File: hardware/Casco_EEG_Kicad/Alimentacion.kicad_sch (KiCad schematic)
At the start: 25 parts, among them J12 USB_B_Micro, Q1 FS8205A, U4 TP4056-42-ESOP8, U5 DW01A, U6 AMS1117-3.3

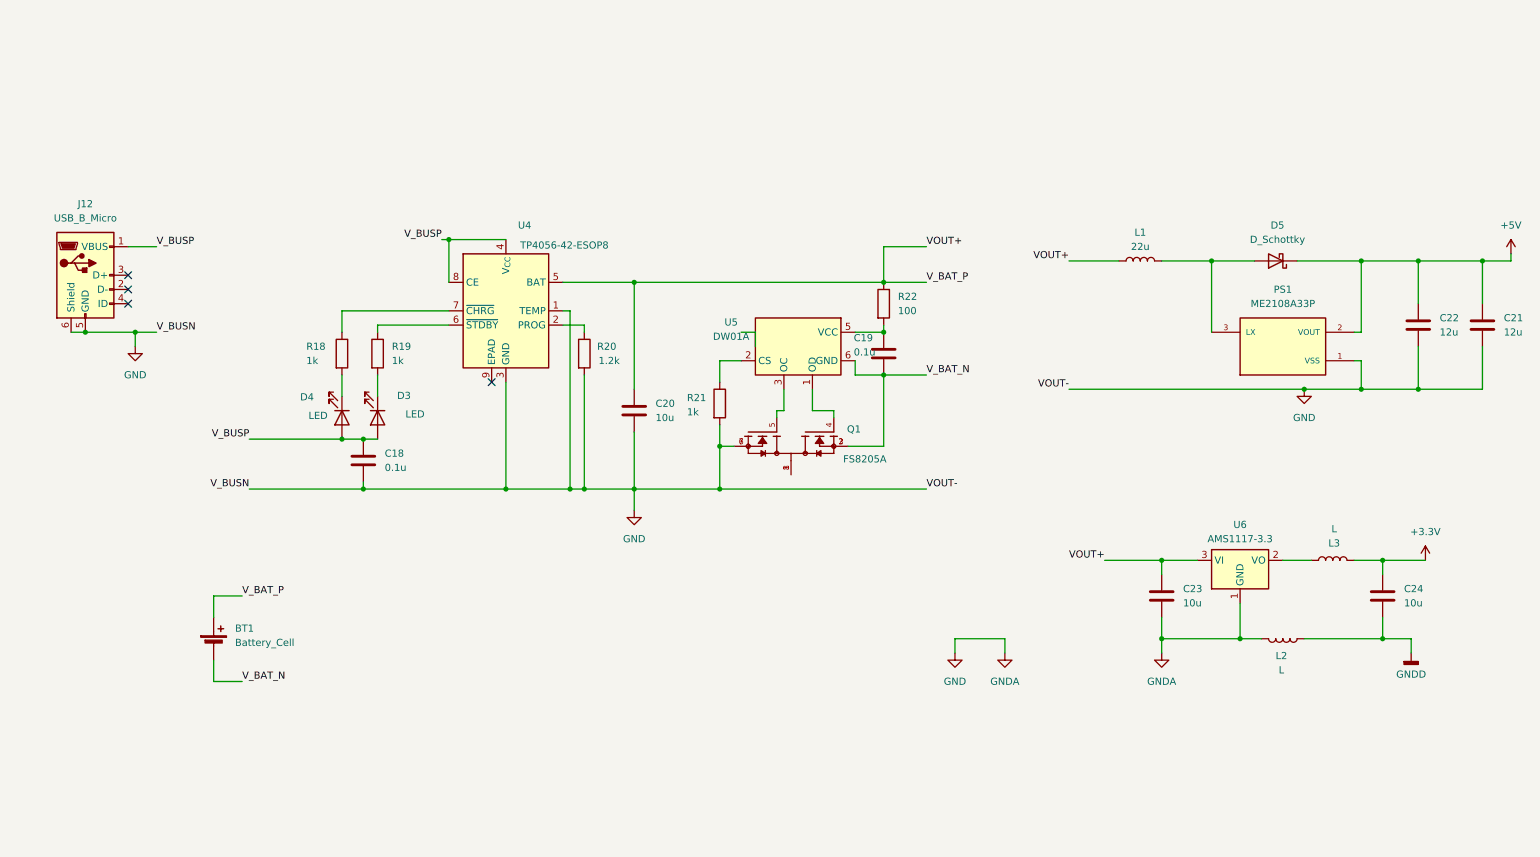
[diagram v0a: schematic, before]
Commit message: Primera implementacion de PCB, cambios varios
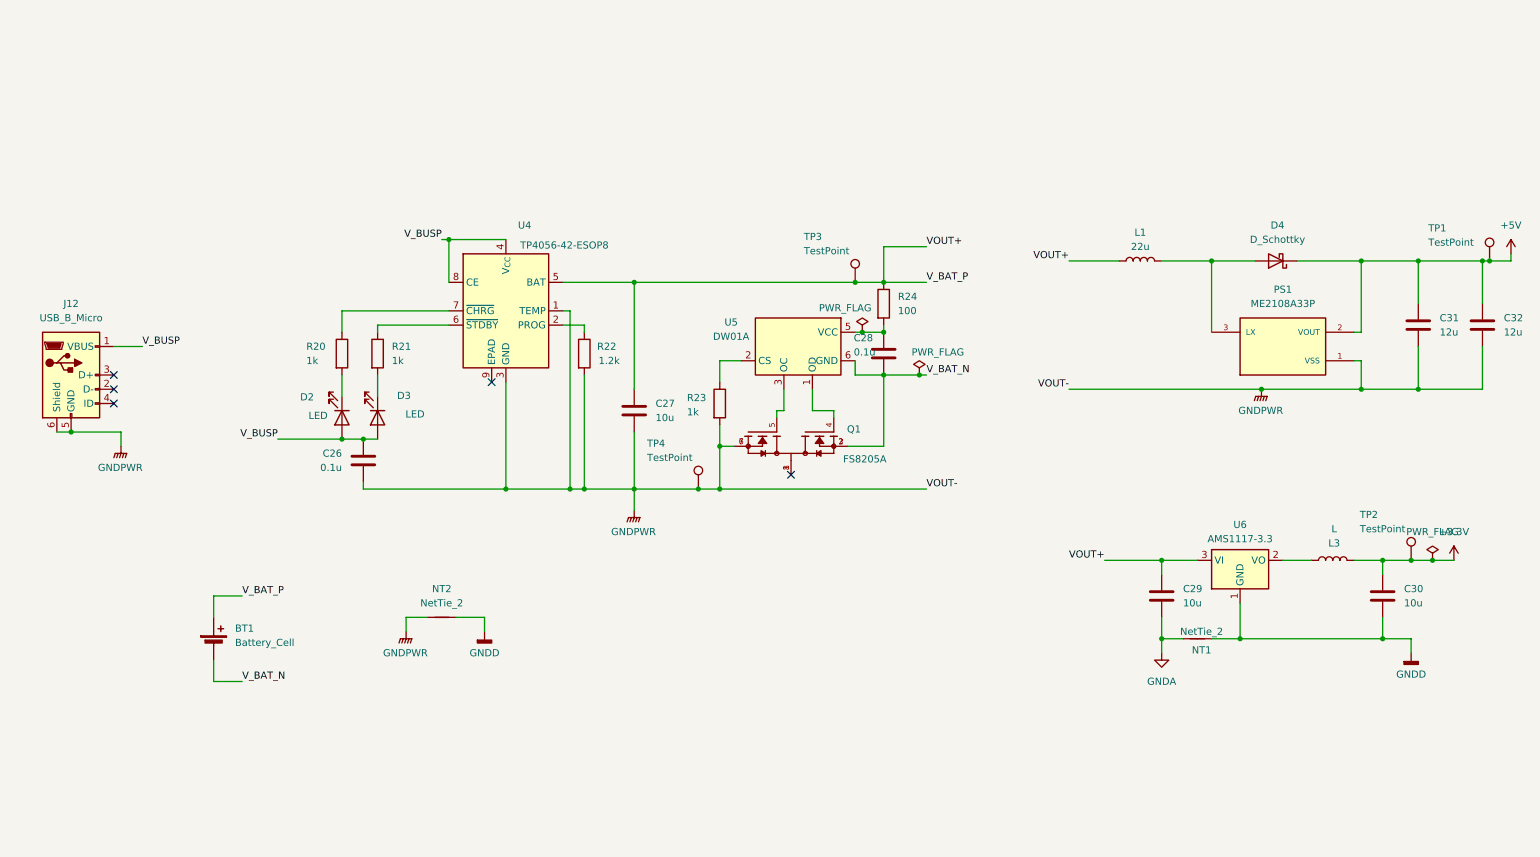
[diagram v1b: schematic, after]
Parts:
- removed L2: L, symbol Device:L
- added NT1, NT2: NetTie_2, NetTie:NetTie-2_SMD_Pad2.0mm, symbol Device:NetTie_2
- added TP1, TP2, TP3, TP4: TestPoint, TestPoint:TestPoint_Pad_D2.0mm, symbol Connector:TestPoint
- C26: renamed from C18; footprint (none) -> Capacitor_SMD:C_0603_1608Metric
- C27: renamed from C20; footprint (none) -> Capacitor_SMD:C_0603_1608Metric
- C28: renamed from C19; footprint (none) -> Capacitor_SMD:C_0603_1608Metric
- C29: renamed from C23; footprint (none) -> Capacitor_SMD:C_0603_1608Metric
- C30: renamed from C24; footprint (none) -> Capacitor_SMD:C_0603_1608Metric
- C31: renamed from C22; footprint (none) -> Capacitor_SMD:C_0805_2012Metric
- C32: renamed from C21; footprint (none) -> Capacitor_SMD:C_0805_2012Metric
- D2: renamed from D4; footprint (none) -> LED_SMD:LED_0603_1608Metric
- D3: footprint (none) -> LED_SMD:LED_0603_1608Metric
- D4: renamed from D5; footprint (none) -> Diode_SMD:D_SMA
- L1: footprint (none) -> Inductor_SMD:L_Coilcraft_XAL5030-XXX
- L3: footprint (none) -> Inductor_SMD:L_Coilcraft_LPS3010
- PS1: footprint ME2108A33P:CONV_ME2108A33P -> Huellas:CONV_ME2108A33P
- Q1: footprint FS8205A:SOP65P640X120-8N -> Huellas:SOP65P640X120-8N
- R20: renamed from R18; footprint (none) -> Resistor_SMD:R_0603_1608Metric
- R21: renamed from R19; footprint Resistor_SMD:R_0201_0603Metric -> Resistor_SMD:R_0603_1608Metric
- R22: renamed from R20; footprint (none) -> Resistor_SMD:R_0603_1608Metric
- R23: renamed from R21; footprint (none) -> Resistor_SMD:R_0603_1608Metric
- R24: renamed from R22; footprint (none) -> Resistor_SMD:R_0603_1608Metric
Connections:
- net +3.3V: now also TP2.1
- net +5V: now also TP1.1
- net GNDD: now also U6.1 (GND), NT1.2, NT2.2
- net VOUT+: now also TP3.1
- net GND renamed GNDPWR
- net GNDPWR: now also NT2.1, TP4.1; no longer C29.2, U6.1 (GND)
- new net GNDA: C29.2, NT1.1
- no-connect marks 4 -> 5
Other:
- moved on the sheet: J12

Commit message: Nuevos cambios al PCB, mejoro planos, regulo 3,3V desde 5V, etc
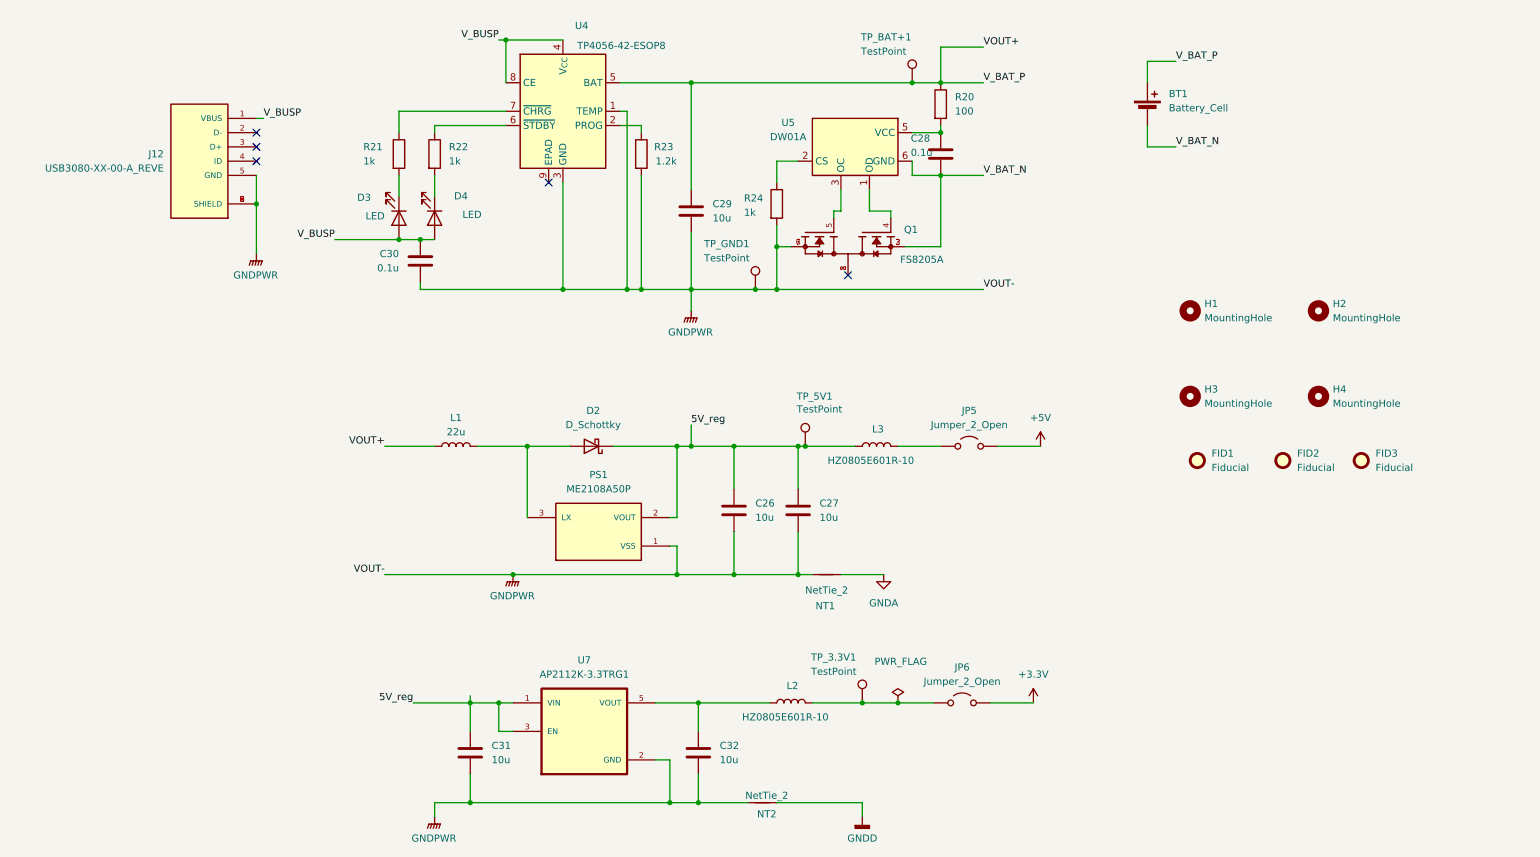
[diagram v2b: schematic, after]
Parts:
- removed J12: USB_B_Micro, Connector_USB:USB_Micro-AB_Molex_47590-0001, symbol Connector:USB_B_Micro
- removed U6: AMS1117-3.3, Package_TO_SOT_SMD:SOT-223-3_TabPin2, symbol Regulator_Linear:AMS1117-3.3
- added FID1, FID2, FID3: Fiducial, Fiducial:Fiducial_0.5mm_Mask1mm, symbol Mechanical:Fiducial
- added H1, H2, H3, H4: MountingHole, MountingHole:MountingHole_2.2mm_M2_Pad_Via, symbol Mechanical:MountingHole
- added J12: USB3080-XX-00-A_REVE, Huellas:GCT_USB3080-XX-00-A_REVE, symbol USBmicroB:USB3080-XX-00-A_REVE
- added JP5, JP6: Jumper_2_Open, Connector_PinHeader_2.54mm:PinHeader_1x02_P2.54mm_Vertical, symbol Jumper:Jumper_2_Open
- added L3: HZ0805E601R-10, Inductor_SMD:L_Eaton_MCL2012V1, symbol Device:L
- added U7: AP2112K-3.3TRG1, Huellas:SOT95P285X140-5N, symbol AP2112K-3.3:AP2112K-3.3TRG1
- C26: renamed from C31; value 12u -> 10u; LCSC PN (none) -> C19702
- C27: renamed from C32; value 12u -> 10u; LCSC PN (none) -> C19702
- C28: LCSC PN (none) -> C48579280
- C29: renamed from C27; LCSC PN (none) -> C19702
- C30: renamed from C26; LCSC PN (none) -> C48579280
- C31: renamed from C29; LCSC PN (none) -> C19702
- C32: renamed from C30; LCSC PN (none) -> C19702
- D2: renamed from D4; LCSC PN (none) -> C2480
- L2: renamed from L3; value L -> HZ0805E601R-10; footprint Inductor_SMD:L_Coilcraft_LPS3010 -> Inductor_SMD:L_Eaton_MCL2012V1; LCSC PN (none) -> C2441364
- PS1: value ME2108A33P -> ME2108A50P; Availability Not in stock -> (none); Check_prices https://www.snapeda.com/parts/ME2108A33P/Nanjing+Micro+One+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 -> (none); LCSC PN (none) -> C236798; MANUFACTURER Nanjing Micro One Electronics -> (none); MP ME2108A33P -> (none); PARTREV V10.0 -> (none); Package Package -> (none); Price None -> (none); STANDARD Manufacturer Recommendations -> (none)
- Q1: LCSC PN (none) -> C2830320
- R20: renamed from R24; LCSC PN (none) -> C22775
- R21: renamed from R20; LCSC PN (none) -> C22548
- R22: renamed from R21; LCSC PN (none) -> C22548
- R23: renamed from R22; LCSC PN (none) -> C22765
- R24: renamed from R23; LCSC PN (none) -> C22548
- U4: LCSC PN (none) -> C16581
- U5: LCSC PN (none) -> C2927799
- renumbered D2 to D3, D3 to D4, NT2 to NT1, NT1 to NT2, TP2 to TP_3.3V1, TP1 to TP_5V1, TP3 to TP_BAT+1, TP4 to TP_GND1
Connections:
- net +3.3V: now also JP6.2 (B); no longer C32.1, L2.2, TP_3.3V1.1
- net +5V: now also JP5.2 (B); no longer C26.1, C27.1, D2.1 (K), PS1.2 (VOUT), TP_5V1.1
- net GNDA: now also NT1.2; no longer C31.2, NT2.1
- net GNDD: no longer C32.2, NT1.2
- net GNDPWR: now also C31.2, C32.2, NT2.1, J12.5 (GND), J12.6 (SHIELD), J12.7 (SHIELD), J12.8 (SHIELD), J12.9 (SHIELD), U7.2 (GND)
- net VOUT+: no longer C31.1
- net V_BUSP: now also J12.1 (VBUS)
- net at L2.1: now also C32.1, U7.5 (VOUT)
- new net: JP5.1 (A), L3.2
- new net: JP6.1 (A), L2.2, TP_3.3V1.1
- new net 5V_reg: C26.1, C27.1, C31.1, D2.1 (K), L3.1, PS1.2 (VOUT), TP_5V1.1, U7.1 (VIN), U7.3 (EN)
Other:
- moved on the sheet: BT1, C26, C27, C28, C29, C30, C31, C32, D2, D3, D4, L1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

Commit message: Implemento pines I/O para trigger
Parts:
- C28, C30: LCSC PN C48579280 -> C14663
- R21, R22, R24: LCSC PN C22548 -> C21190
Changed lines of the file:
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@@
 			)
 		)
-		(property "LCSC PN" "C48579280"
+		(property "LCSC PN" "C14663"
 			(at 82.55 64.77 0)
 			(effects
@@
 			)
 		)
-		(property "LCSC PN" "C22548"
+		(property "LCSC PN" "C21190"
 			(at 146.05 54.61 0)
 			(effects
@@
 			)
 		)
-		(property "LCSC PN" "C48579280"
+		(property "LCSC PN" "C14663"
 			(at 175.26 45.72 0)
 			(effects
@@
 			)
 		)
-		(property "LCSC PN" "C22548"
+		(property "LCSC PN" "C21190"
 			(at 78.74 45.72 0)
 			(effects
@@
 			)
 		)
-		(property "LCSC PN" "C22548"
+		(property "LCSC PN" "C21190"
 			(at 85.09 45.72 0)
 			(effects

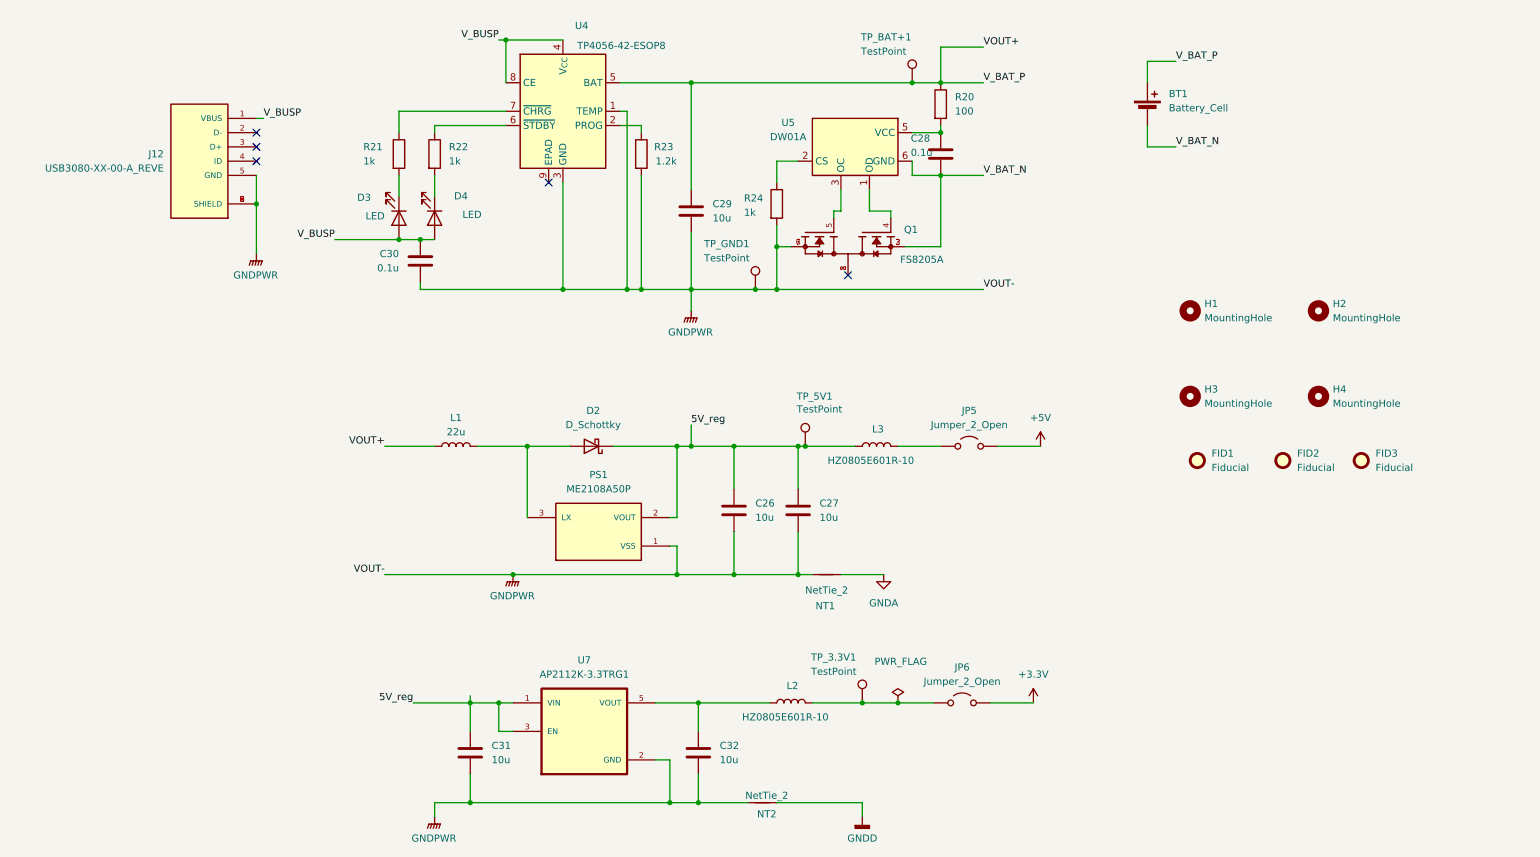
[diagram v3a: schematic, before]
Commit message: Actualizacion del modelo, agrego mini slide switch, agrego jumpers para comunicacion con modulo BT
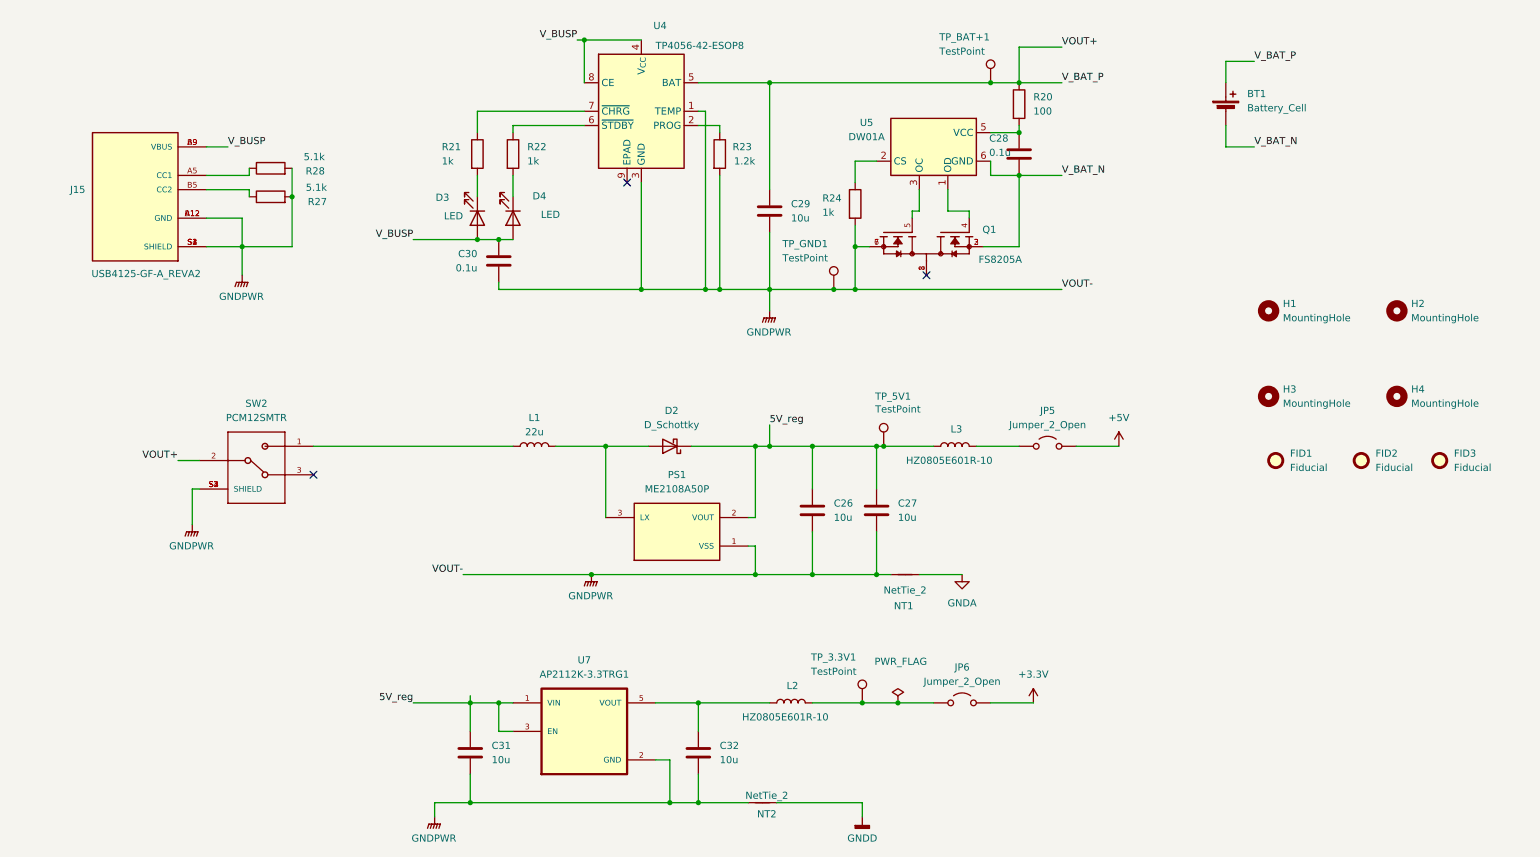
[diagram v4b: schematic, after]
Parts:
- removed J12: USB3080-XX-00-A_REVE, Huellas:GCT_USB3080-XX-00-A_REVE, symbol USBmicroB:USB3080-XX-00-A_REVE
- added J15: USB4125-GF-A_REVA2, Huellas:GCT_USB4125-GF-A_REVA2, symbol USBmicroC:USB4125-GF-A_REVA2
- added R27, R28: 5.1k, Resistor_SMD:R_0603_1608Metric, symbol Device:R
- added SW2: PCM12SMTR, Huellas:SW_PCM12SMTR, symbol MiniSwitch:PCM12SMTR
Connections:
- net GNDPWR: now also J15.A12 (GND), J15.B12 (GND), J15.S1 (SHIELD), J15.S2 (SHIELD), J15.S3 (SHIELD), J15.S4 (SHIELD), R27.2, R28.2, SW2.S1 (SHIELD), SW2.S2 (SHIELD), SW2.S3 (SHIELD), SW2.S4 (SHIELD)
- net VOUT+: now also SW2.2; no longer L1.1
- net V_BUSP: now also J15.A9 (VBUS), J15.B9 (VBUS)
- new net: J15.B5 (CC2), R27.1
- new net: J15.A5 (CC1), R28.1
- new net: L1.1, SW2.1
- no-connect marks 5 -> 3
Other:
- moved on the sheet: BT1, C26, C27, C28, C29, C30, D2, D3, D4, FID1, FID2, FID3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
